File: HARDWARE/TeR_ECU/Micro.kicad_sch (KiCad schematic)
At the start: 23 parts, among them J4 Debug, SW1 RST, U3 STM32F446RETx, Y1 Crystal

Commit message: Contuinuando con Layout, micro hecha
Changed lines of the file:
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@@
   (no_connect (at 170.18 114.3))
   (no_connect (at 170.18 119.38))
-  (no_connect (at 134.62 80.01))
+  (no_connect (at 134.62 81.28))
   (no_connect (at 134.62 78.74))
   (no_connect (at 170.18 81.28))

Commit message: avanzando
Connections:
- net BL: now also U3.24 (PC4); no longer U3.52 (PC11)
- net Horn: now also U3.25 (PC5); no longer U3.53 (PC12)
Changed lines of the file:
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@@
   (no_connect (at 134.62 114.3))
   (no_connect (at 170.18 55.88))
-  (no_connect (at 134.62 91.44))
+  (no_connect (at 134.62 109.22))
   (no_connect (at 170.18 93.98))
   (no_connect (at 170.18 73.66))
@@
   (no_connect (at 170.18 99.06))
   (no_connect (at 134.62 73.66))
-  (no_connect (at 134.62 88.9))
+  (no_connect (at 134.62 106.68))
   (no_connect (at 170.18 116.84))
   (no_connect (at 170.18 58.42))
@@
     (stroke (width 0) (type default))
   )
-  (wire (pts (xy 124.46 106.68) (xy 134.62 106.68))
-    (stroke (width 0) (type default))
-  )
   (wire (pts (xy 34.29 31.75) (xy 44.45 31.75))
     (stroke (width 0) (type default))
@@
     (stroke (width 0) (type default))
   )
+  (wire (pts (xy 130.81 91.44) (xy 134.62 91.44))
+    (stroke (width 0) (type default))
+  )
   (wire (pts (xy 33.02 173.99) (xy 34.29 173.99))
     (stroke (width 0) (type default))
@@
     (stroke (width 0) (type default))
   )
-  (wire (pts (xy 124.46 109.22) (xy 134.62 109.22))
-    (stroke (width 0) (type default))
-  )
   (wire (pts (xy 154.94 50.8) (xy 154.94 46.99))
     (stroke (width 0) (type default))
@@
   )
   (wire (pts (xy 15.24 31.75) (xy 24.13 31.75))
+    (stroke (width 0) (type default))
+  )
+  (wire (pts (xy 130.81 88.9) (xy 134.62 88.9))
     (stroke (width 0) (type default))
   )
@@
     (effects (font (size 1.27 1.27)) (justify left bottom))
   )
-  (hierarchical_label "Horn" (shape output) (at 124.46 109.22 180) (fields_autoplaced)
+  (hierarchical_label "Horn" (shape output) (at 130.81 91.44 180) (fields_autoplaced)
     (effects (font (size 1.27 1.27)) (justify right))
   )
@@
     (effects (font (size 1.27 1.27)) (justify left))
   )
-  (hierarchical_label "BL" (shape output) (at 124.46 106.68 180) (fields_autoplaced)
+  (hierarchical_label "BL" (shape output) (at 130.81 88.9 180) (fields_autoplaced)
     (effects (font (size 1.27 1.27)) (justify right))
   )

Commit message: Falta poco
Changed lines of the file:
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@@
+    (stroke (width 0) (type default))
+  )
+  (wire (pts (xy 124.46 88.9) (xy 134.62 88.9))
     (stroke (width 0) (type default))
   )
@@
     (stroke (width 0) (type default))
   )
-  (wire (pts (xy 130.81 91.44) (xy 134.62 91.44))
-    (stroke (width 0) (type default))
-  )
   (wire (pts (xy 33.02 173.99) (xy 34.29 173.99))
     (stroke (width 0) (type default))
@@
     (stroke (width 0) (type default))
   )
-  (wire (pts (xy 130.81 88.9) (xy 134.62 88.9))
-    (stroke (width 0) (type default))
-  )
   (wire (pts (xy 60.96 128.27) (xy 60.96 127))
     (stroke (width 0) (type default))
@@
   )
   (wire (pts (xy 266.7 30.48) (xy 260.35 30.48))
+    (stroke (width 0) (type default))
+  )
+  (wire (pts (xy 124.46 91.44) (xy 134.62 91.44))
     (stroke (width 0) (type default))
   )
@@
     (effects (font (size 1.27 1.27)) (justify left bottom))
   )
-  (hierarchical_label "Horn" (shape output) (at 130.81 91.44 180) (fields_autoplaced)
+  (hierarchical_label "Horn" (shape output) (at 124.46 91.44 180) (fields_autoplaced)
     (effects (font (size 1.27 1.27)) (justify right))
   )
@@
     (effects (font (size 1.27 1.27)) (justify left))
   )
-  (hierarchical_label "BL" (shape output) (at 130.81 88.9 180) (fields_autoplaced)
+  (hierarchical_label "BL" (shape output) (at 124.46 88.9 180) (fields_autoplaced)
     (effects (font (size 1.27 1.27)) (justify right))
   )

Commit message: Falta Conector
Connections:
- net CAN2_RX: now also U3.57 (PB5); no longer U3.33 (PB12)
- net CAN2_TX: now also U3.58 (PB6); no longer U3.34 (PB13)
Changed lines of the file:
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@@
   (no_connect (at 134.62 83.82))
   (no_connect (at 170.18 134.62))
-  (no_connect (at 170.18 114.3))
+  (no_connect (at 170.18 129.54))
   (no_connect (at 170.18 119.38))
   (no_connect (at 134.62 81.28))
@@
   (no_connect (at 170.18 124.46))
   (no_connect (at 170.18 63.5))
-  (no_connect (at 170.18 111.76))
+  (no_connect (at 170.18 127))
   (no_connect (at 170.18 60.96))
   (no_connect (at 170.18 109.22))
@@
   (no_connect (at 170.18 132.08))
   (no_connect (at 170.18 76.2))
-  (no_connect (at 170.18 120.65))
+  (no_connect (at 170.18 121.92))
   (no_connect (at 170.18 101.6))
   (no_connect (at 134.62 111.76))
@@
     (stroke (width 0) (type default))
   )
+  (wire (pts (xy 170.18 111.76) (xy 177.8 111.76))
+    (stroke (width 0) (type default))
+  )
   (wire (pts (xy 24.13 24.13) (xy 34.29 24.13))
     (stroke (width 0) (type default))
@@
     (stroke (width 0) (type default))
   )
-  (wire (pts (xy 170.18 129.54) (xy 177.8 129.54))
-    (stroke (width 0) (type default))
-  )
   (wire (pts (xy 45.72 173.99) (xy 48.26 173.99))
     (stroke (width 0) (type default))
@@
     (stroke (width 0) (type default))
   )
-  (wire (pts (xy 170.18 127) (xy 177.8 127))
-    (stroke (width 0) (type default))
-  )
   (wire (pts (xy 59.69 173.99) (xy 64.77 173.99))
+    (stroke (width 0) (type default))
+  )
+  (wire (pts (xy 170.18 114.3) (xy 177.8 114.3))
     (stroke (width 0) (type default))
   )
@@
     (effects (font (size 1.27 1.27)) (justify left))
   )
-  (hierarchical_label "CAN2_RX" (shape input) (at 177.8 127 0) (fields_autoplaced)
+  (hierarchical_label "CAN2_RX" (shape input) (at 177.8 111.76 0) (fields_autoplaced)
     (effects (font (size 1.27 1.27)) (justify left))
   )
-  (hierarchical_label "CAN2_TX" (shape output) (at 177.8 129.54 0) (fields_autoplaced)
+  (hierarchical_label "CAN2_TX" (shape output) (at 177.8 114.3 0) (fields_autoplaced)
     (effects (font (size 1.27 1.27)) (justify left))
   )

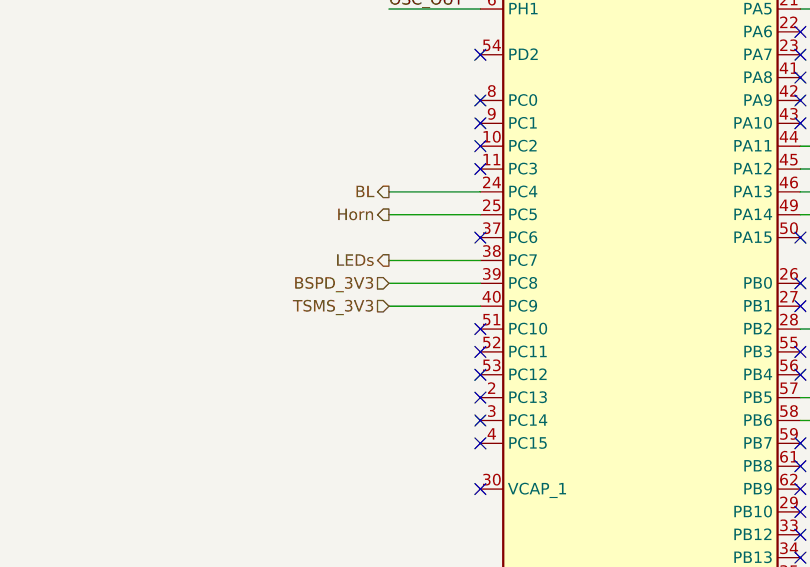
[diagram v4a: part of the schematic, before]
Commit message: Falta pinear conector
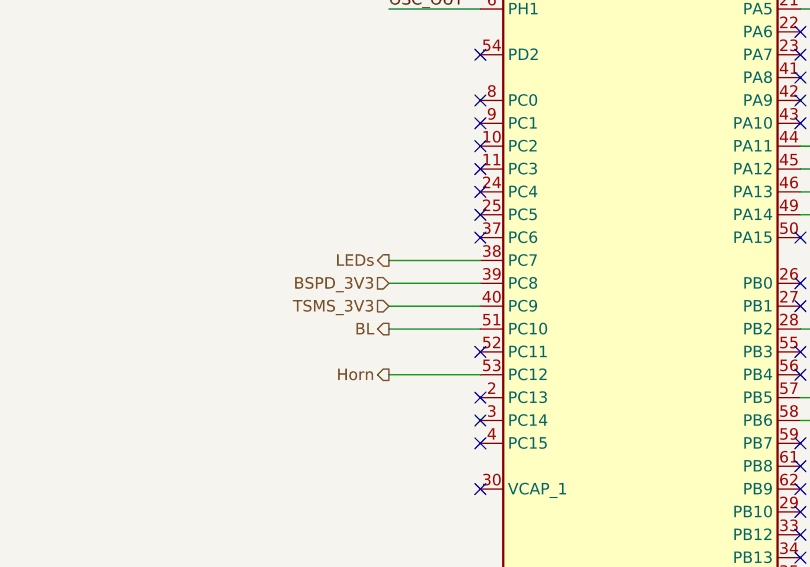
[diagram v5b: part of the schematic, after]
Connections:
- net BL: now also U3.51 (PC10); no longer U3.24 (PC4)
- net Horn: now also U3.53 (PC12); no longer U3.25 (PC5)
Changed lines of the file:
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@@
   (no_connect (at 134.62 114.3))
   (no_connect (at 170.18 55.88))
-  (no_connect (at 134.62 109.22))
+  (no_connect (at 134.62 91.44))
   (no_connect (at 170.18 93.98))
   (no_connect (at 170.18 73.66))
@@
   (no_connect (at 170.18 101.6))
   (no_connect (at 134.62 111.76))
-  (no_connect (at 134.62 104.14))
+  (no_connect (at 134.62 88.9))
   (no_connect (at 170.18 99.06))
   (no_connect (at 134.62 73.66))
@@
     (stroke (width 0) (type default))
   )
+  (wire (pts (xy 124.46 109.22) (xy 134.62 109.22))
+    (stroke (width 0) (type default))
+  )
   (wire (pts (xy 124.46 68.58) (xy 134.62 68.58))
     (stroke (width 0) (type default))
@@
     (stroke (width 0) (type default))
   )
+  (wire (pts (xy 124.46 104.14) (xy 134.62 104.14))
+    (stroke (width 0) (type default))
+  )
   (wire (pts (xy 55.88 55.88) (xy 55.88 57.15))
     (stroke (width 0) (type default))
   )
-  (wire (pts (xy 124.46 88.9) (xy 134.62 88.9))
-    (stroke (width 0) (type default))
-  )
   (polyline (pts (xy 12.7 149.86) (xy 74.93 149.86))
     (stroke (width 0) (type default))
@@
     (stroke (width 0) (type default))
   )
+  (wire (pts (xy 170.18 114.3) (xy 177.8 114.3))
+    (stroke (width 0) (type default))
+  )
   (polyline (pts (xy 74.93 12.7) (xy 74.93 40.64))
     (stroke (width 0) (type default))
@@
     (stroke (width 0) (type default))
   )
-  (wire (pts (xy 124.46 91.44) (xy 134.62 91.44))
-    (stroke (width 0) (type default))
-  )
   (wire (pts (xy 157.48 46.99) (xy 154.94 46.99))
     (stroke (width 0) (type default))
@@
   )
   (wire (pts (xy 59.69 173.99) (xy 64.77 173.99))
-    (stroke (width 0) (type default))
-  )
-  (wire (pts (xy 170.18 114.3) (xy 177.8 114.3))
     (stroke (width 0) (type default))
   )
@@
     (effects (font (size 1.27 1.27)) (justify left bottom))
   )
-  (hierarchical_label "Horn" (shape output) (at 124.46 91.44 180) (fields_autoplaced)
+  (hierarchical_label "Horn" (shape output) (at 124.46 109.22 180) (fields_autoplaced)
     (effects (font (size 1.27 1.27)) (justify right))
   )
@@
     (effects (font (size 1.27 1.27)) (justify left))
   )
-  (hierarchical_label "BL" (shape output) (at 124.46 88.9 180) (fields_autoplaced)
+  (hierarchical_label "BL" (shape output) (at 124.46 104.14 180) (fields_autoplaced)
     (effects (font (size 1.27 1.27)) (justify right))
   )

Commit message: Solo falta revisar
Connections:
- net BL: now also U3.50 (PA15); no longer U3.51 (PC10)
- net UART_RX: now reaches U3.52 (PC11)
- new net UART_TX: U3.51 (PC10)
- no-connect marks 35 -> 33
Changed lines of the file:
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@@
   (no_connect (at 170.18 55.88))
   (no_connect (at 134.62 91.44))
-  (no_connect (at 170.18 93.98))
   (no_connect (at 170.18 73.66))
   (no_connect (at 134.62 121.92))
@@
   (no_connect (at 170.18 99.06))
   (no_connect (at 134.62 73.66))
-  (no_connect (at 134.62 106.68))
   (no_connect (at 170.18 116.84))
   (no_connect (at 170.18 58.42))
@@
     (stroke (width 0) (type default))
   )
+  (wire (pts (xy 55.88 55.88) (xy 55.88 57.15))
+    (stroke (width 0) (type default))
+  )
+  (polyline (pts (xy 12.7 149.86) (xy 74.93 149.86))
+    (stroke (width 0) (type default))
+  )
+  (wire (pts (xy 27.94 88.9) (xy 31.75 88.9))
+    (stroke (width 0) (type default))
+  )
+  (wire (pts (xy 152.4 143.51) (xy 152.4 144.78))
+    (stroke (width 0) (type default))
+  )
   (wire (pts (xy 124.46 104.14) (xy 134.62 104.14))
     (stroke (width 0) (type default))
   )
-  (wire (pts (xy 55.88 55.88) (xy 55.88 57.15))
-    (stroke (width 0) (type default))
-  )
-  (polyline (pts (xy 12.7 149.86) (xy 74.93 149.86))
-    (stroke (width 0) (type default))
-  )
-  (wire (pts (xy 27.94 88.9) (xy 31.75 88.9))
-    (stroke (width 0) (type default))
-  )
-  (wire (pts (xy 152.4 143.51) (xy 152.4 144.78))
-    (stroke (width 0) (type default))
-  )
   (wire (pts (xy 44.45 31.75) (xy 54.61 31.75))
     (stroke (width 0) (type default))
@@
     (stroke (width 0) (type default))
   )
+  (wire (pts (xy 124.46 106.68) (xy 134.62 106.68))
+    (stroke (width 0) (type default))
+  )
   (wire (pts (xy 34.29 31.75) (xy 44.45 31.75))
     (stroke (width 0) (type default))
@@
   )
   (wire (pts (xy 54.61 31.75) (xy 64.77 31.75))
+    (stroke (width 0) (type default))
+  )
+  (wire (pts (xy 170.18 93.98) (xy 177.8 93.98))
     (stroke (width 0) (type default))
   )
@@
     (effects (font (size 1.27 1.27)) (justify right))
   )
+  (hierarchical_label "UART_TX" (shape output) (at 124.46 104.14 180) (fields_autoplaced)
+    (effects (font (size 1.27 1.27)) (justify right))
+  )
   (hierarchical_label "SWCLK" (shape output) (at 177.8 91.44 0) (fields_autoplaced)
     (effects (font (size 1.27 1.27)) (justify left))
@@
     (effects (font (size 1.27 1.27)) (justify left))
   )
-  (hierarchical_label "BL" (shape output) (at 124.46 104.14 180) (fields_autoplaced)
-    (effects (font (size 1.27 1.27)) (justify right))
+  (hierarchical_label "BL" (shape output) (at 177.8 93.98 0) (fields_autoplaced)
+    (effects (font (size 1.27 1.27)) (justify left))
   )
   (hierarchical_label "SWDIO" (shape output) (at 177.8 88.9 0) (fields_autoplaced)
@@
     (effects (font (size 1.27 1.27)) (justify right))
   )
+  (hierarchical_label "UART_RX" (shape input) (at 124.46 106.68 180) (fields_autoplaced)
+    (effects (font (size 1.27 1.27)) (justify right))
+  )

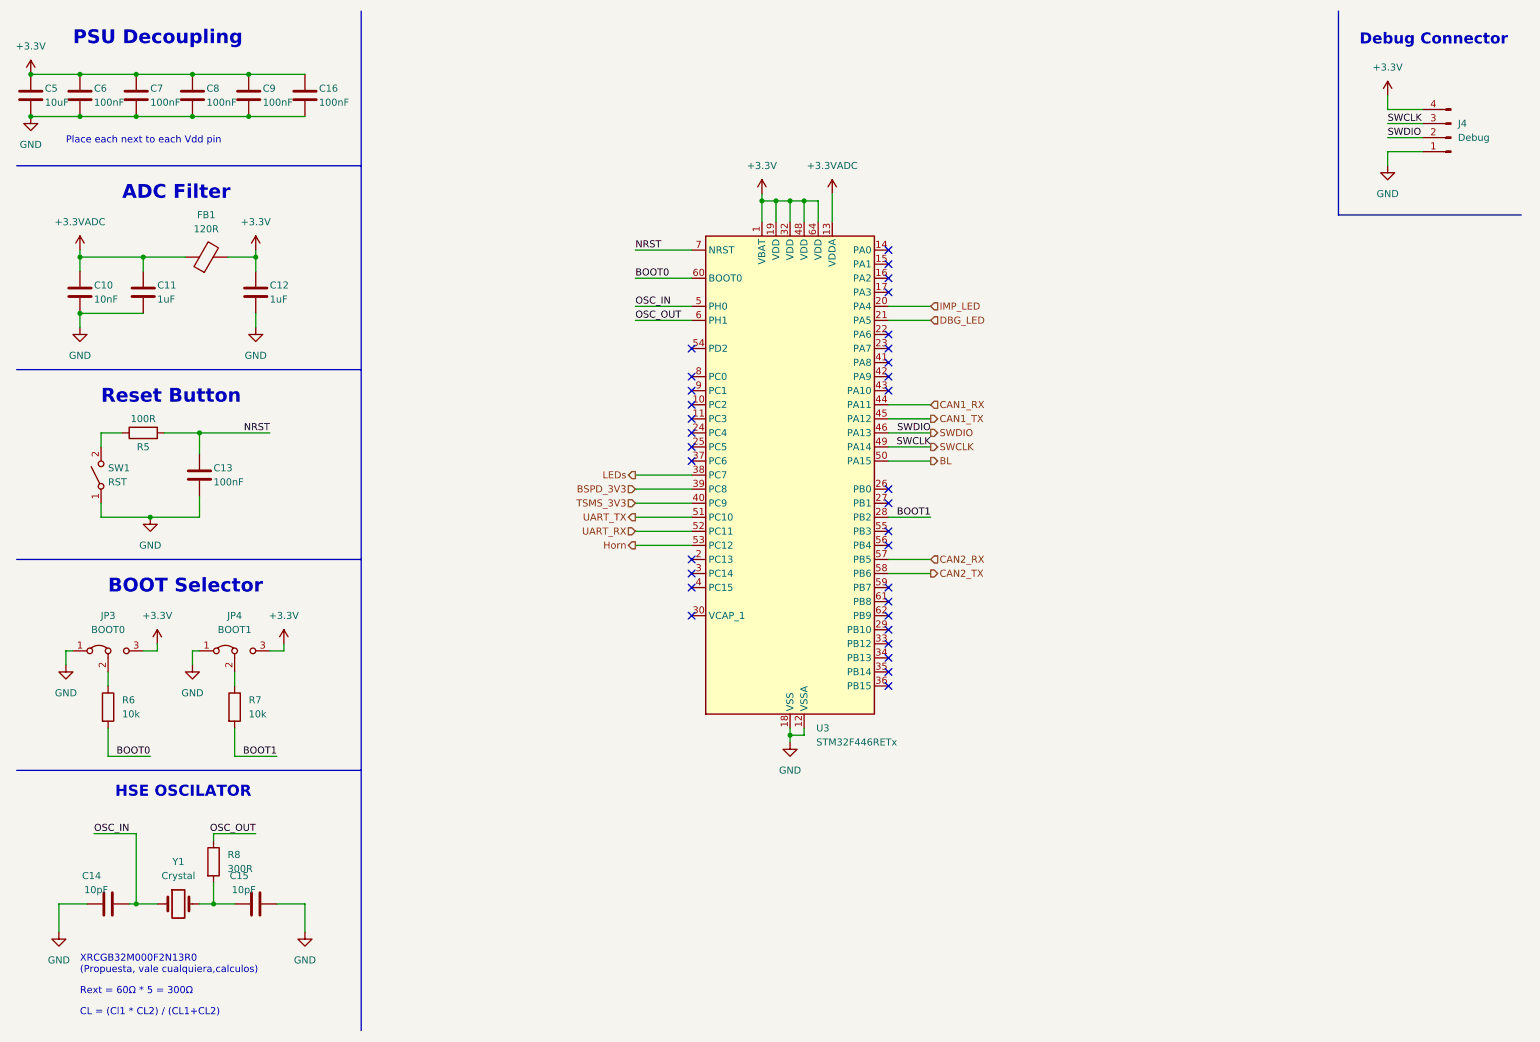
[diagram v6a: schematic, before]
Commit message: Rethought layout and footprints and fixed fuse normative problem
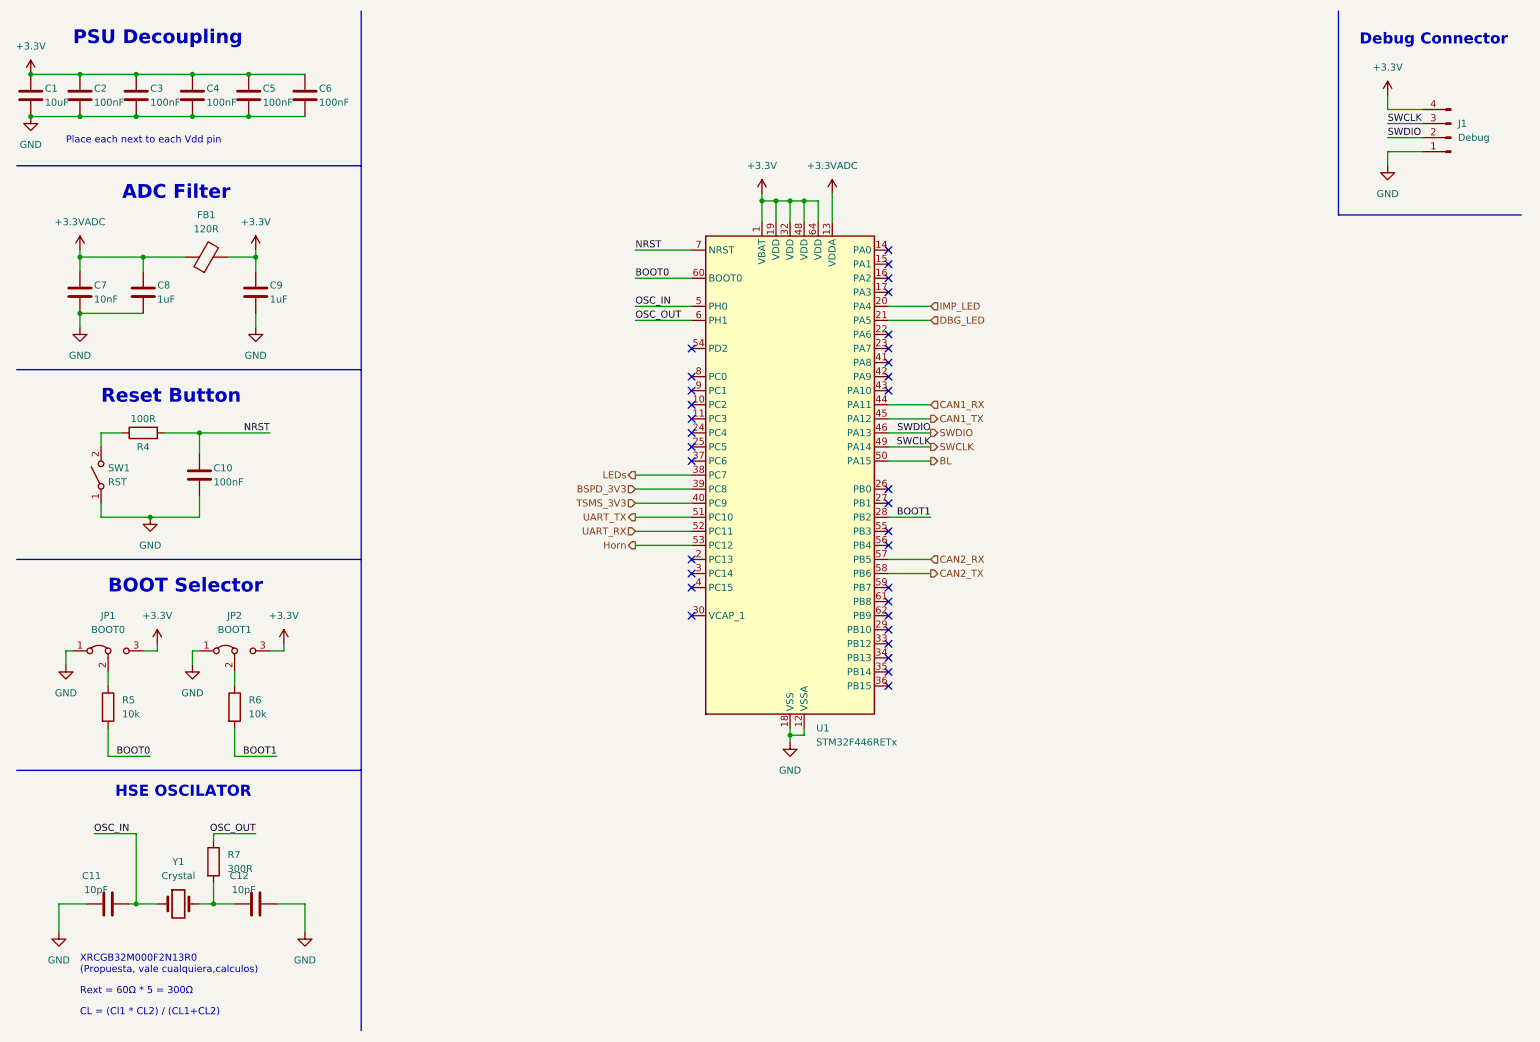
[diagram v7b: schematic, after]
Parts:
- C2: renamed from C6; footprint Capacitor_SMD:C_0805_2012Metric -> Capacitor_SMD:C_0402_1005Metric
- C3: renamed from C7; footprint Capacitor_SMD:C_0805_2012Metric -> Capacitor_SMD:C_0402_1005Metric
- C4: renamed from C8; footprint Capacitor_SMD:C_0805_2012Metric -> Capacitor_SMD:C_0402_1005Metric
- C5: renamed from C9; footprint Capacitor_SMD:C_0805_2012Metric -> Capacitor_SMD:C_0402_1005Metric
- C7: renamed from C10; footprint Capacitor_SMD:C_0402_1005Metric_Pad0.74x0.62mm_HandSolder -> Capacitor_SMD:C_0603_1608Metric
- C8: renamed from C11; footprint Capacitor_SMD:C_0402_1005Metric_Pad0.74x0.62mm_HandSolder -> Capacitor_SMD:C_0603_1608Metric
- C9: renamed from C12; footprint Capacitor_SMD:C_0402_1005Metric_Pad0.74x0.62mm_HandSolder -> Capacitor_SMD:C_0603_1608Metric
- renumbered C5 to C1, C13 to C10, C14 to C11, C15 to C12, C16 to C6, J4 to J1, JP3 to JP1, JP4 to JP2, R5 to R4, R6 to R5, R7 to R6, R8 to R7, U3 to U1
